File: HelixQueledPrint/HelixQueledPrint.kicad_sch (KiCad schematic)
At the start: 44 parts, among them J1 USB_C_Receptacle_USB2.0_16P, J101 Conn_Coaxial, SW1 SW_SPST, SW2 SW_SPST, U101 ESP32-C6FHx, U102 BGS12WN6E6327, Y1 40MHz

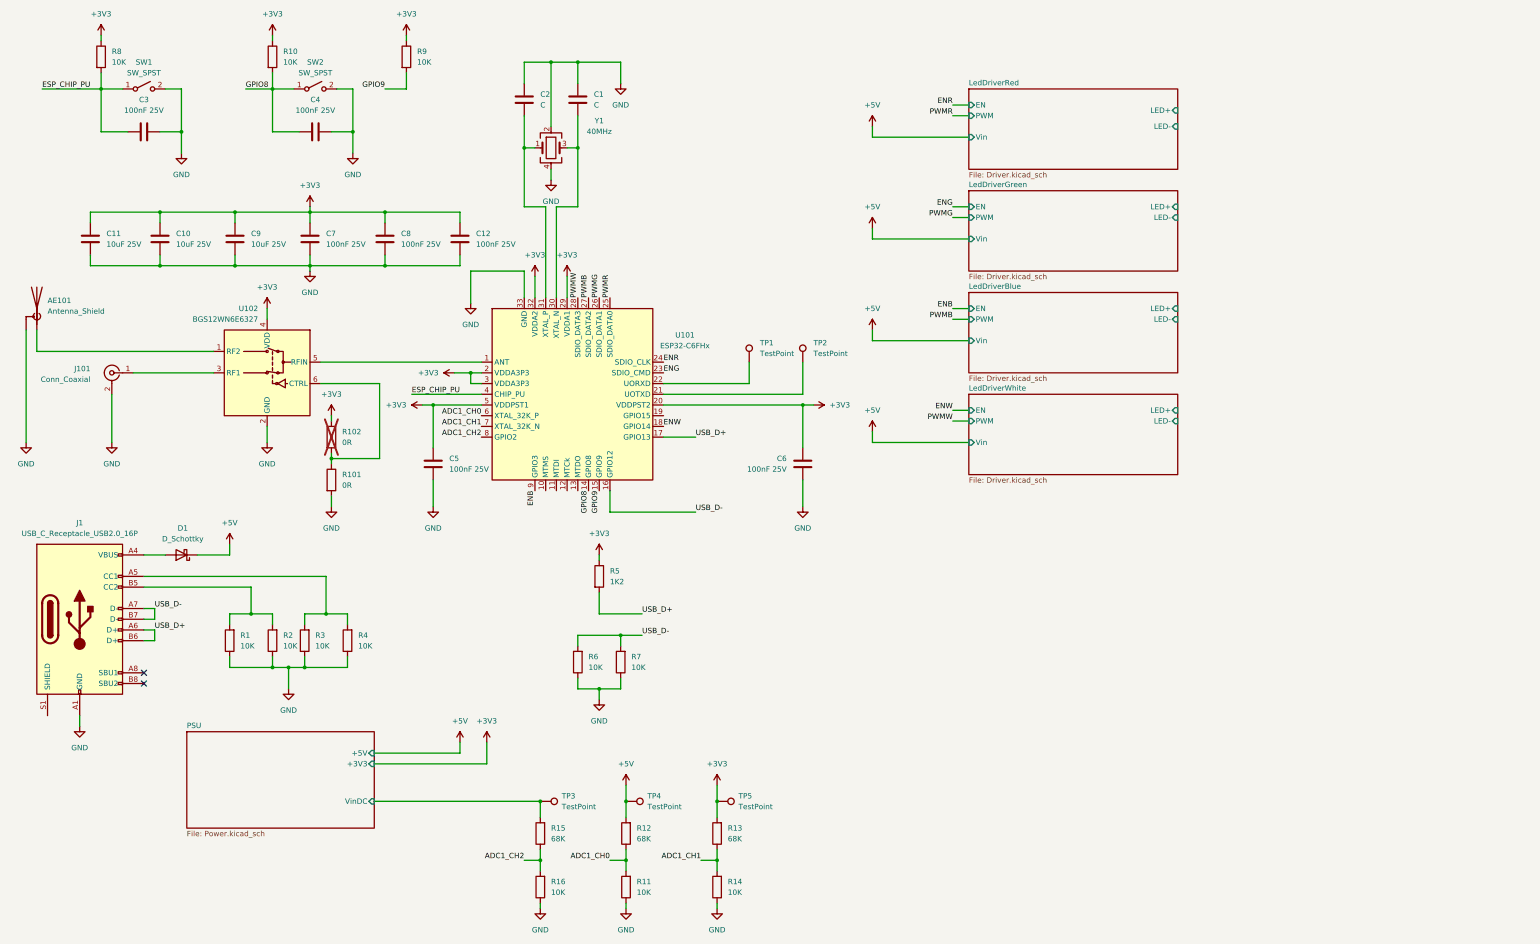
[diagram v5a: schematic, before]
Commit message: footprints toegewezen
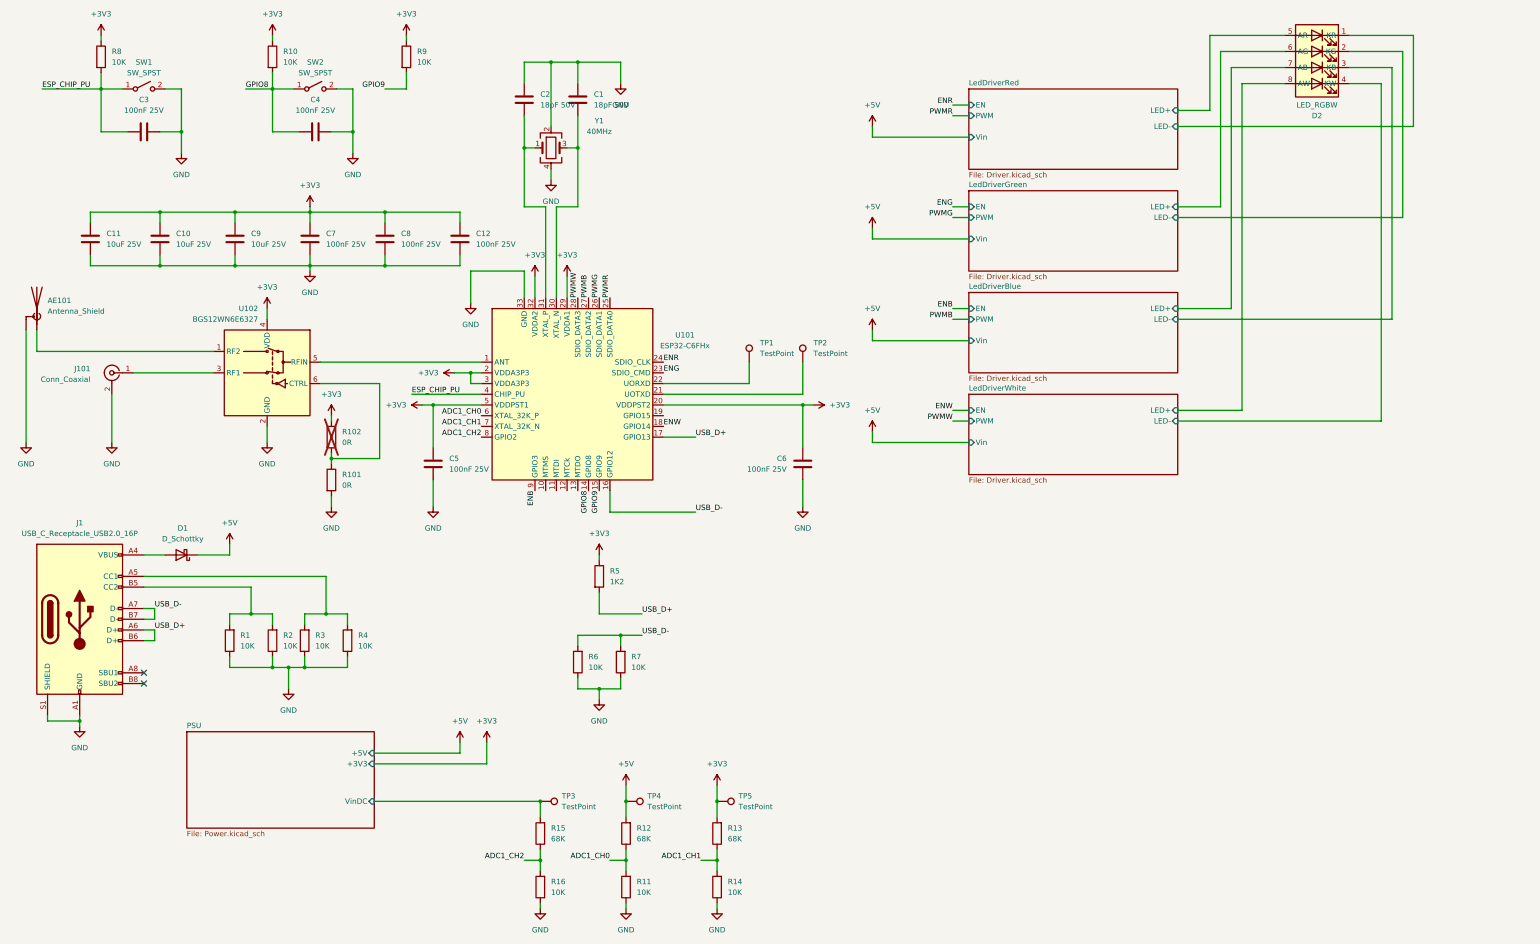
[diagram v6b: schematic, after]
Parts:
- added D2: LED_RGBW, symbol 1CustomSymbols:LED_RGBW_8P
- AE101: footprint (none) -> RF_Antenna:Texas_SWRA117D_2.4GHz_Left
- C1, C2: value C -> 18pF 50V; footprint (none) -> Capacitor_SMD:C_0402_1005Metric
- D1: footprint (none) -> Diode_SMD:D_SOD-110; MPN (none) -> CUS10S30,H3F
- J1: footprint (none) -> Connector_USB:USB_C_Receptacle_GCT_USB4105-xx-A_16P_TopMnt_Horizontal
- J101: footprint (none) -> Connector_Coaxial:U.FL_Hirose_U.FL-R-SMT-1_Vertical; MPN (none) -> RF1-2626-125CE-CT
- R1, R10, R101, R102, R11, R12, R13, R14, R15, R16, R2, R3, R4, R5, R6, R7, R8, R9: footprint (none) -> Resistor_SMD:R_0402_1005Metric
- SW1, SW2: footprint (none) -> 1CustomFootprints:TS1101A26025; MPN (none) -> GT-TC034A-H025-L1NB
- TP1, TP2, TP3, TP4, TP5: footprint (none) -> TestPoint:TestPoint_Pad_D1.0mm
- Y1: footprint (none) -> Crystal:Crystal_SMD_3225-4Pin_3.2x2.5mm_HandSoldering; MPN (none) -> C37635388
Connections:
- net GND: now also J1.S1 (SHIELD)
- net LedDriverBlue/LED+: now also D2.7 (AB)
- net LedDriverBlue/LED-: now also D2.3 (KB)
- net LedDriverGreen/LED+: now also D2.6 (AG)
- net LedDriverGreen/LED-: now also D2.2 (KG)
- net LedDriverRed/LED+: now also D2.5 (AR)
- net LedDriverRed/LED-: now also D2.1 (KR)
- net LedDriverWhite/LED+: now also D2.8 (AW)
- net LedDriverWhite/LED-: now also D2.4 (KW)

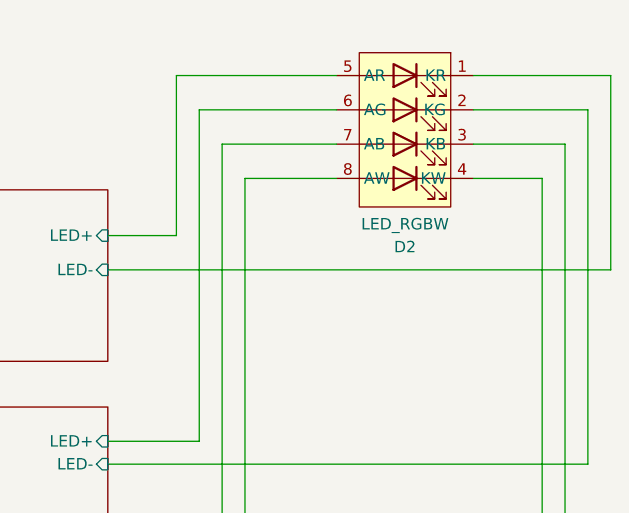
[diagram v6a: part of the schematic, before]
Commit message: Netklases toegevoegd, componenten naar pcb geplaatst
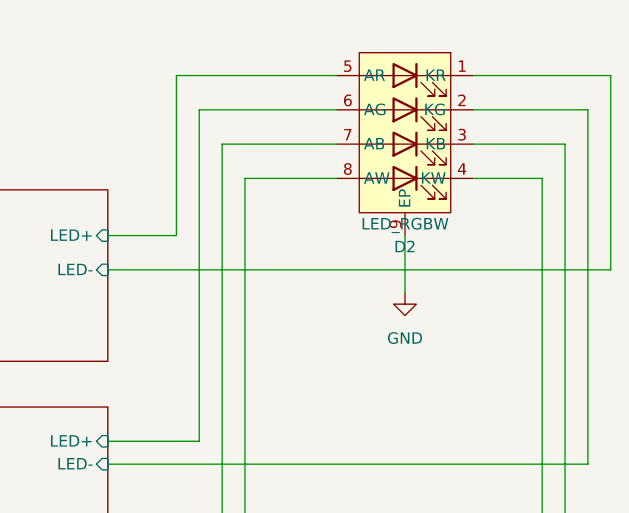
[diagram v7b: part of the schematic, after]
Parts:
- D2: footprint (none) -> 1CustomFootprints:QR4xLED
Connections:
- net GND: now also D2.9 (EP)
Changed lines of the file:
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@@
 	(wire
 		(pts
+			(xy 328.93 40.64) (xy 328.93 46.99)
+		)
+		(stroke
+			(width 0)
+			(type default)
+		)
+	)
+	(wire
+		(pts
 			(xy 125.73 77.47) (xy 107.95 77.47)
 		)
@@
 		)
 	)
+	(netclass_flag ""
+		(length 2.54)
+		(shape round)
+		(at 52.2035 102.87 0)
+		(fields_autoplaced yes)
+		(effects
+			(font
+				(size 1.27 1.27)
+			)
+			(justify left bottom)
+		)
+		(property "Netclass" "RF"
+			(at 52.902 100.33 0)
+			(effects
+				(font
+					(size 1.27 1.27)
+				)
+				(justify left)
+			)
+		)
+		(property "Component Class" ""
+			(at -197.9865 10.16 0)
+			(effects
+				(font
+					(size 1.27 1.27)
+					(italic yes)
+				)
+			)
+		)
+	)
+	(netclass_flag ""
+		(length 2.54)
+		(shape round)
+		(at 101.6 100.33 0)
+		(fields_autoplaced yes)
+		(effects
+			(font
+				(size 1.27 1.27)
+			)
+			(justify left bottom)
+		)
+		(property "Netclass" "RF"
+			(at 102.2985 97.79 0)
+			(effects
+				(font
+					(size 1.27 1.27)
+				)
+				(justify left)
+			)
+		)
+		(property "Component Class" ""
+			(at -148.59 7.62 0)
+			(effects
+				(font
+					(size 1.27 1.27)
+					(italic yes)
+				)
+			)
+		)
+	)
+	(netclass_flag ""
+		(length 2.54)
+		(shape round)
+		(at 163.83 165.1 0)
+		(fields_autoplaced yes)
+		(effects
+			(font
+				(size 1.27 1.27)
+			)
+			(justify left bottom)
+		)
+		(property "Netclass" "USB"
+			(at 164.5285 162.56 0)
+			(effects
+				(font
+					(size 1.27 1.27)
+				)
+				(justify left)
+			)
+		)
+		(property "Component Class" ""
+			(at -87.63 73.66 0)
+			(effects
+				(font
+					(size 1.27 1.27)
+					(italic yes)
+				)
+			)
+		)
+	)
+	(netclass_flag ""
+		(length 2.54)
+		(shape round)
+		(at 50.8 97.79 0)
+		(fields_autoplaced yes)
+		(effects
+			(font
+				(size 1.27 1.27)
+			)
+			(justify left bottom)
+		)
+		(property "Netclass" "RF"
+			(at 51.4985 95.25 0)
+			(effects
+				(font
+					(size 1.27 1.27)
+				)
+				(justify left)
+			)
+		)
+		(property "Component Class" ""
+			(at -199.39 5.08 0)
+			(effects
+				(font
+					(size 1.27 1.27)
+					(italic yes)
+				)
+			)
+		)
+	)
+	(netclass_flag ""
+		(length 2.54)
+		(shape round)
+		(at 163.83 160.02 0)
+		(fields_autoplaced yes)
+		(effects
+			(font
+				(size 1.27 1.27)
+			)
+			(justify left bottom)
+		)
+		(property "Netclass" "USB"
+			(at 164.5285 157.48 0)
+			(effects
+				(font
+					(size 1.27 1.27)
+				)
+				(justify left)
+			)
+		)
+		(property "Component Class" ""
+			(at -87.63 68.58 0)
+			(effects
+				(font
+					(size 1.27 1.27)
+					(italic yes)
+				)
+			)
+		)
+	)
 	(symbol
 		(lib_id "Device:R")
@@
 	)
 	(symbol
+		(lib_id "power:GND")
+		(at 328.93 46.99 0)
+		(mirror y)
+		(unit 1)
+		(exclude_from_sim no)
+		(in_bom yes)
+		(on_board yes)
+		(dnp no)
+		(fields_autoplaced yes)
+		(property "Reference" "#PWR033"
+			(at 328.93 53.34 0)
+			(effects
+				(font
+					(size 1.27 1.27)
+				)
+				(hide yes)
+			)
+		)
+		(property "Value" "GND"
+			(at 328.93 52.07 0)
+			(effects
+				(font
+					(size 1.27 1.27)
+				)
+			)
+		)
+		(property "Footprint" ""
+			(at 328.93 46.99 0)
+			(effects
+				(font
+					(size 1.27 1.27)
+				)
+				(hide yes)
+			)
+		)
+		(property "Datasheet" ""
+			(at 328.93 46.99 0)
+			(effects
+				(font
+					(size 1.27 1.27)
+				)
+				(hide yes)
+			)
+		)
+		(property "Description" "Power symbol creates a global label with name \"GND\" , ground"
+			(at 328.93 46.99 0)
+			(effects
+				(font
+					(size 1.27 1.27)
+				)
+				(hide yes)
+			)
+		)
+		(pin "1"
+		)
+		(instances
+			(project "HelixQueledPrint"
+				(path "/398fd733-417c-46a8-b62a-83839861ebca"
+					(reference "#PWR033")
+					(unit 1)
+				)
+			)
+		)
+	)
+	(symbol
 		(lib_id "Device:R")
 		(at 158.75 151.13 0)
@@
 			)
 		)
-		(property "Footprint" ""
+		(property "Footprint" "1CustomFootprints:QR4xLED"
 			(at 328.93 29.21 0)
 			(effects
@@
 		(pin "1"
 		)
+		(pin "9"
+		)
 		(instances
